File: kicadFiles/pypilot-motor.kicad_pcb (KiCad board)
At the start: 2 copper layers, 80 x 33.9 mm, 22 parts, among them J11 Motor B, J12 GND, J13 GND, J4 12V, J5 12V, J7 1x4, J8 Motor A, J9 End Stops

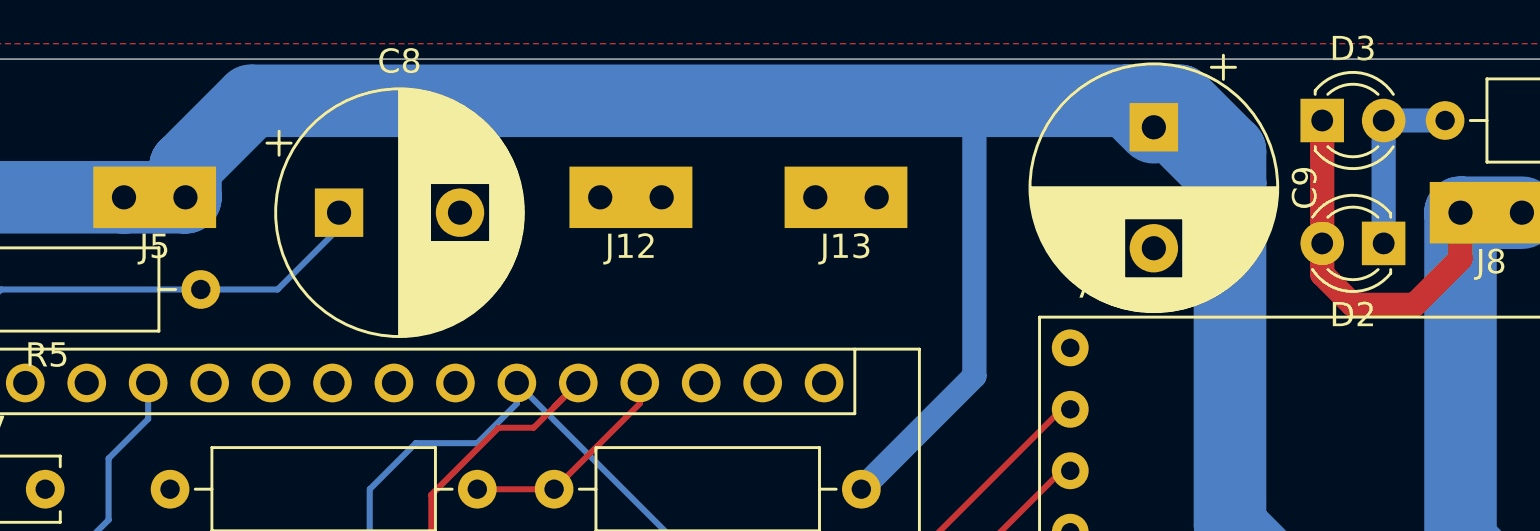
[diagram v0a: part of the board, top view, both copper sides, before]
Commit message: 2nd Fix Problem where motor wrongly report 170°C due to error in wiring
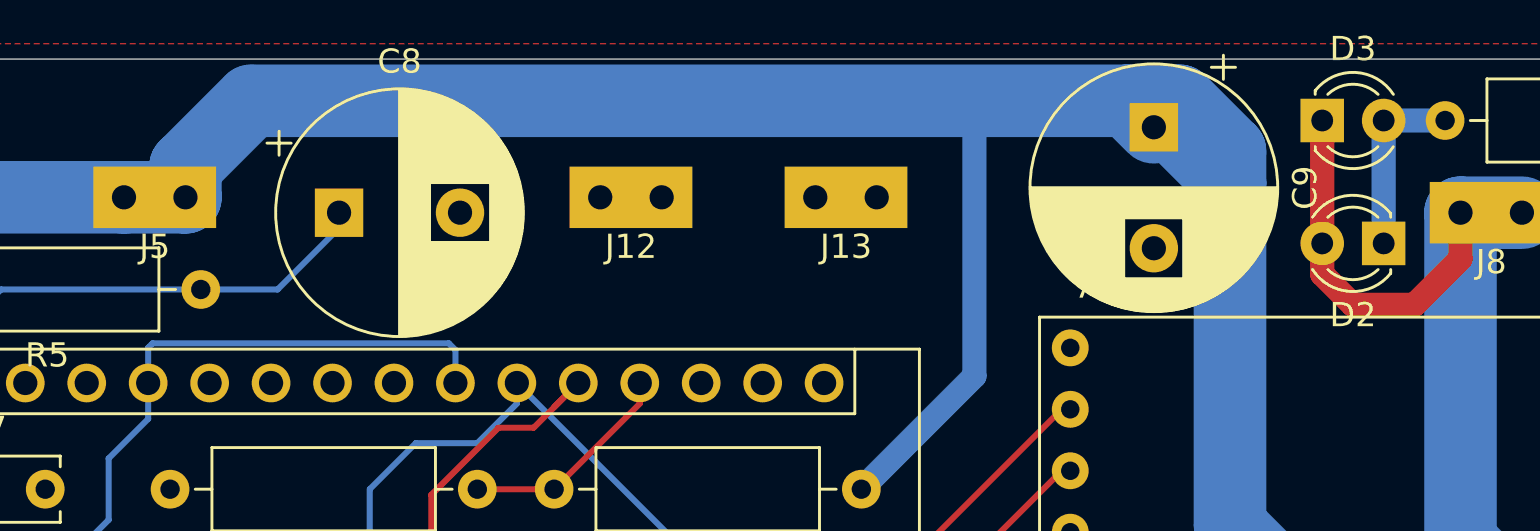
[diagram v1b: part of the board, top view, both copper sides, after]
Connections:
- net ~SLP renamed ~{SLP}
- A3 pad 22: GND -> Net-(A3-Pad27)
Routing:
- net Net-(A3-Pad27): track 10.9 -> 26.7 mm
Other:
- net class Default removed
- net class power removed
